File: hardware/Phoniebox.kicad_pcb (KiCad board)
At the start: 2 copper layers, 64.8 x 66 mm, 75 parts, among them J1 GPIO, J2 Screw_Terminal_01x08, J3 Screw_Terminal_01x08, J4 Screw_Terminal_01x08, J5 Conn_01x02, J6 Conn_02x06_Odd_Even, J8 Conn_01x08, Q1 2N7002, Q2 2N7002, Q3 2N7002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

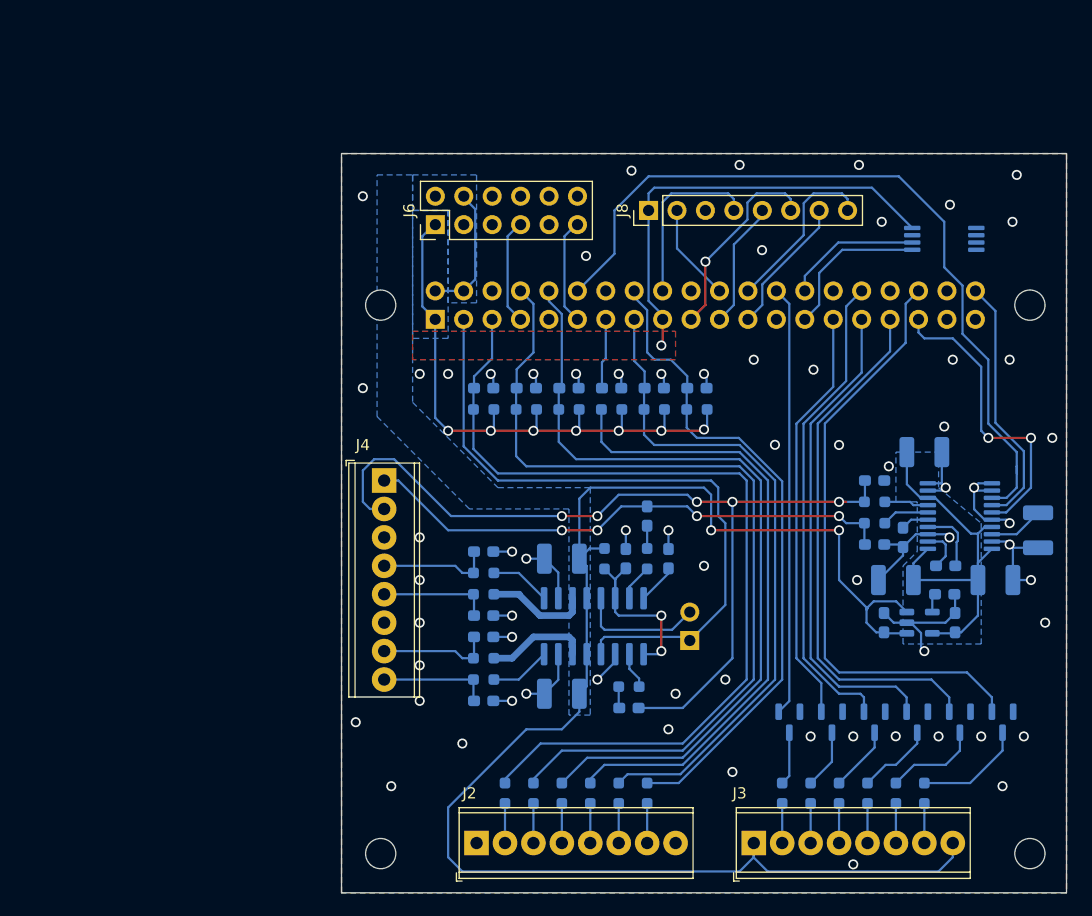
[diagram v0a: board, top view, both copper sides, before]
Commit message: Add OnOff-SHIM circuit to PCB
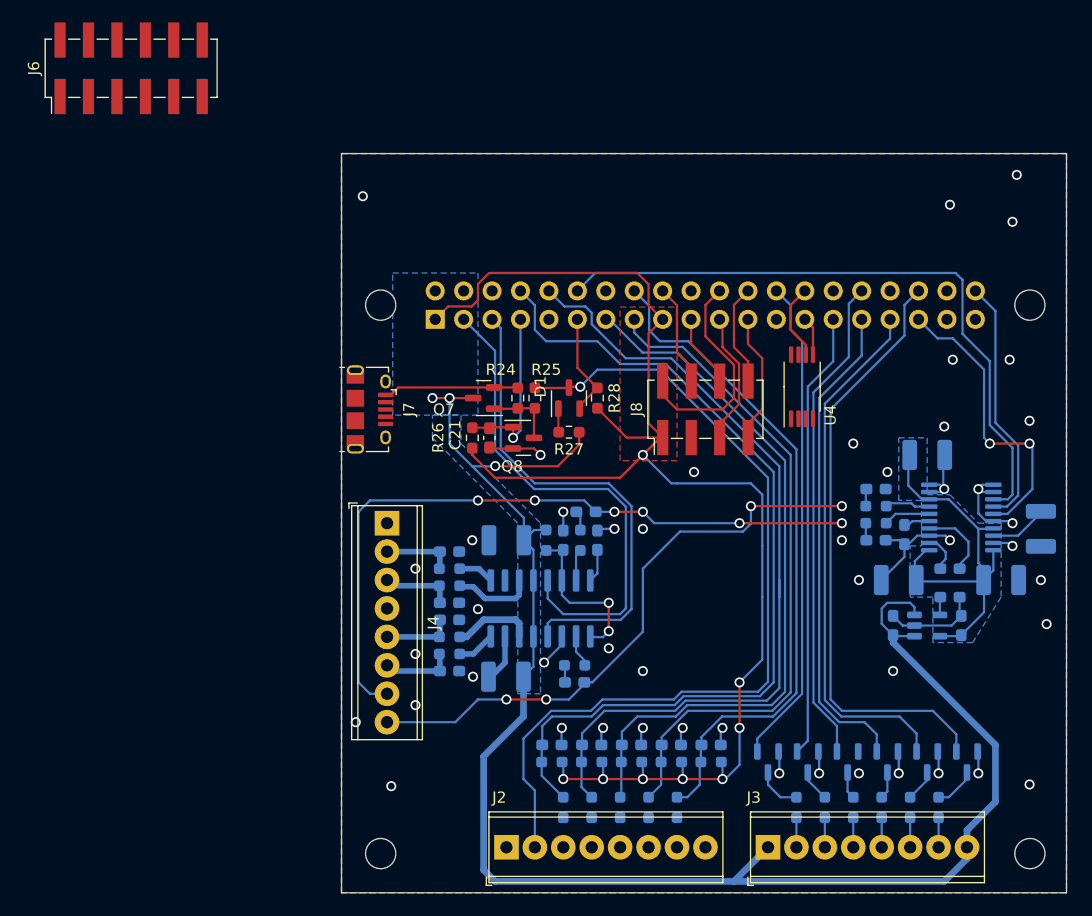
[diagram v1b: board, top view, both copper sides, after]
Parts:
- removed C1: 1n, Capacitor_SMD:C_0603_1608Metric_Pad1.08x0.95mm_HandSolder
- removed J5: Conn_01x02, Connector_PinHeader_2.54mm:PinHeader_1x02_P2.54mm_Vertical
- removed R1: 10k, Resistor_SMD:R_0603_1608Metric_Pad0.98x0.95mm_HandSolder
- removed R2: 100, Resistor_SMD:R_0603_1608Metric_Pad0.98x0.95mm_HandSolder
- added C21: 4u7, Capacitor_SMD:C_0603_1608Metric_Pad1.08x0.95mm_HandSolder, F.Cu at (113.2, 59.4)
- added D1: BAT54C, Package_TO_SOT_SMD:SOT-23, F.Cu at (120.3, 55.8)
- added J7: USB_B_Micro, Connector_USB:USB_Micro-B_Amphenol_10118194_Horizontal, F.Cu at (102.5, 56.8)
- added Q7: AO3401A, Package_TO_SOT_SMD:SOT-23, F.Cu at (112.7, 55.8)
- added Q8: 2N7002, Package_TO_SOT_SMD:SOT-23, F.Cu at (116.3, 59.4)
- added R24: 100k, Resistor_SMD:R_0603_1608Metric_Pad0.98x0.95mm_HandSolder, F.Cu at (115.7, 55.8)
- added R25: 10k, Resistor_SMD:R_0603_1608Metric_Pad0.98x0.95mm_HandSolder, F.Cu at (117.3, 55.8)
- added R26: 1k, Resistor_SMD:R_0603_1608Metric_Pad0.98x0.95mm_HandSolder, F.Cu at (111.7, 59.4)
- added R27: 1k, Resistor_SMD:R_0603_1608Metric_Pad0.98x0.95mm_HandSolder, F.Cu at (120.3, 58.9)
- added R28: 1k, Resistor_SMD:R_0603_1608Metric_Pad0.98x0.95mm_HandSolder, F.Cu at (122.9, 55.8)
- J6: footprint Connector_PinHeader_2.54mm:PinHeader_2x06_P2.54mm_Vertical -> Connector_PinHeader_2.54mm:PinHeader_2x06_P2.54mm_Vertical_SMD
- J8: value Conn_01x08 -> Conn_02x04_Odd_Even; footprint Connector_PinHeader_2.54mm:PinHeader_1x08_P2.54mm_Vertical -> Connector_PinHeader_2.54mm:PinHeader_2x04_P2.54mm_Vertical_SMD
- U4: moved to F.Cu
- moved C8 32.0 mm to (118.8, 86.8)
- moved C9 31.9 mm to (122.4, 86.8)
- moved C14 31.9 mm to (125.9, 86.8)
- moved C15 31.9 mm to (129.5, 86.8)
- moved C16 31.9 mm to (133.0, 86.8)
- moved R6 31.6 mm to (118.8, 88.3)
- moved R8 31.6 mm to (122.4, 88.3)
- moved R10 31.5 mm to (125.9, 88.3)
- moved R12 31.5 mm to (129.5, 88.3)
- moved R20 31.5 mm to (133.0, 88.3)
- moved J6 30.6 mm to (81.2, 26.3)
- moved J8 18.5 mm to (132.5, 56.8)
- moved U4 18.3 mm to (141.1, 54.8), turned to 90 degrees
- moved C6 6.56 mm to (122.9, 68.5)
- moved R3 6.19 mm to (121.3, 68.5)
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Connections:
- J1 pad 11: /Trigger -> /GPIO17_Trigger
- J1 pad 7: /Power_Cut -> /GPIO4_PowerOff
- J4 pad 1: /INL -> GND
- J4 pad 2: /INR -> /SPK_L+
- J4 pad 3: GND -> /SPK_L-
- J4 pad 4: /SPK_L+ -> GND
- J4 pad 5: /SPK_L- -> /SPK_R-
- J4 pad 6: GND -> /SPK_R+
- J4 pad 7: /SPK_R- -> /INL
- J4 pad 8: /SPK_R+ -> /INR
- U1 pad 12: /GPIO2 -> /GPIO3
- U1 pad 5: /~{MUTE} -> /GPIO2
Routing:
- net /Button_1: track 3.53 -> 77.8 mm, vias 0 -> 1
- net /GPIO3: track 81.3 -> 44.2 mm
- net +3V3: track 94.1 -> 125.5 mm
- net /INR: track 80.2 -> 54.5 mm, vias 5 -> 4
- net /INL: track 48.2 -> 64.9 mm, vias 4 -> 6
- net /GPIO4_PowerOff: track 0.00 -> 15.5 mm, vias 0 -> 1
- net /GPIO2: track 60.3 -> 45.0 mm
- net /GPIO18: track 70.6 -> 58.3 mm
- net /VBUS: track 0.00 -> 12.1 mm
- net /MOSI: track 18.0 -> 6.57 mm, vias 1 -> 0
- net /~{MUTE}: track 11.2 -> 0.00 mm
- net /RST: track 8.76 -> 19.7 mm
- net GND: track 79.8 -> 69.4 mm, vias 67 -> 47
- net /ID_SDA: track 13.8 -> 3.46 mm
- net /GPIO17_Trigger: track 0.00 -> 9.37 mm
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- removed copper zone on B.Cu, net +3V3

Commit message: Fix DRC errors/warnings, Add round edges for PCB.
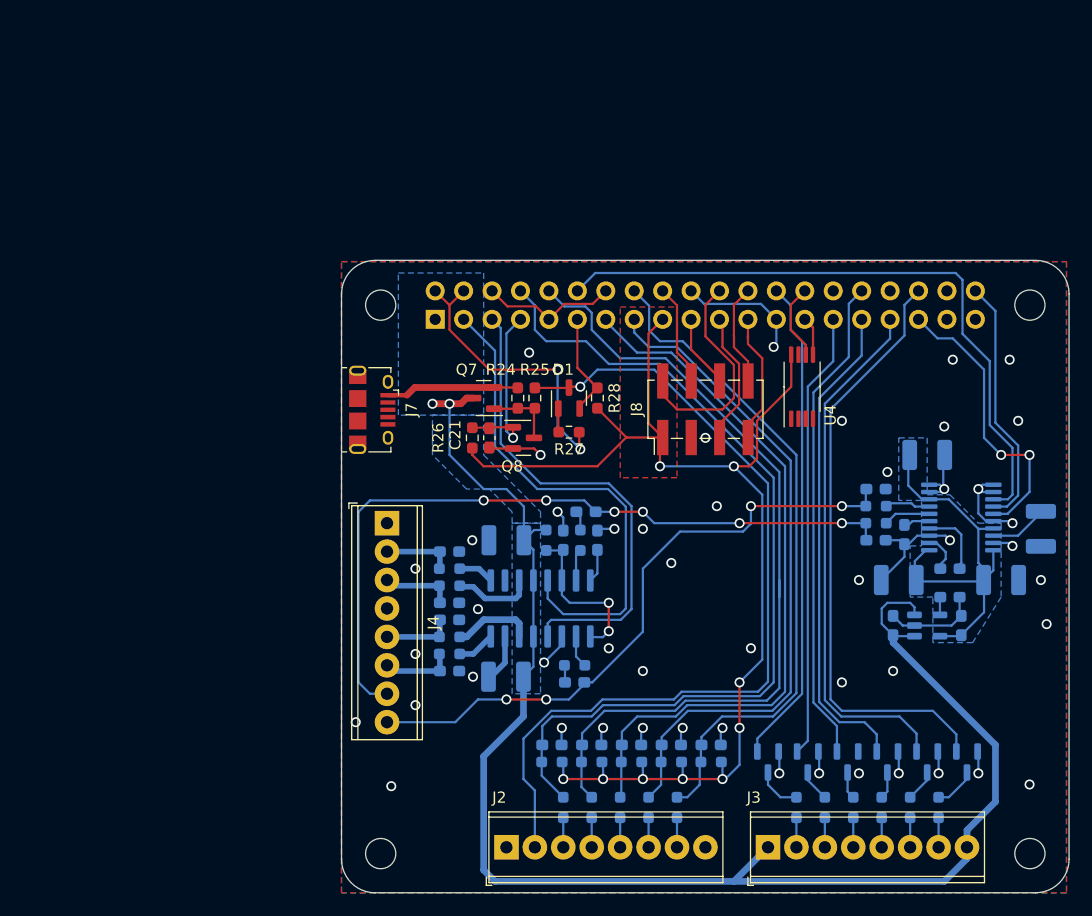
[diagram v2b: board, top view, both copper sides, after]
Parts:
- removed J6: Conn_02x06_Odd_Even, Connector_PinHeader_2.54mm:PinHeader_2x06_P2.54mm_Vertical_SMD
- moved J7 0.21 mm to (102.8, 56.8)
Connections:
- J1 pad 1: +3V3 -> unconnected-(J1-Pad1)
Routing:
- net GND: track 69.4 -> 92.3 mm, vias 47 -> 49
- net +3V3: track 125.5 -> 109.3 mm, vias 8 -> 9
- net +5V: track 146.9 -> 162.8 mm
- net /Button_6: track 0.00 -> 2.64 mm
- net /Button_5: track 0.00 -> 2.64 mm
- net /Button_4: track 0.00 -> 2.64 mm
- net /Button_3: track 0.00 -> 2.64 mm
- net /Button_2: track 0.00 -> 2.64 mm
- net /INR: track 54.5 -> 56.6 mm
- net /INL: track 64.9 -> 66.3 mm
- net /GPIO19: track 26.7 -> 25.9 mm
- net Net-(C24-Pad2): track 6.71 -> 6.18 mm
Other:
- board size 64.8 x 66 mm -> 65 x 56.5 mm

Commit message: Create hierachical schematic sheets for audio/LED/buttons.
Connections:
- net /AVDD renamed /Audio/AVDD
- net /INL1 renamed /Audio/INL1
- net /INL2 renamed /Audio/INL2
- net /INR1 renamed /Audio/INR1
- net /INR2 renamed /Audio/INR2
- net /LOUT+ renamed /Audio/LOUT+
- net /LOUT- renamed /Audio/LOUT-
- net /OUTL renamed /Audio/OUTL
- net /OUTR renamed /Audio/OUTR
- net /ROUT+ renamed /Audio/ROUT+
- net /ROUT- renamed /Audio/ROUT-
- net Net-(C25-Pad1) renamed /Audio/VNEG
- net Net-(C26-Pad1) renamed /Audio/LDOO

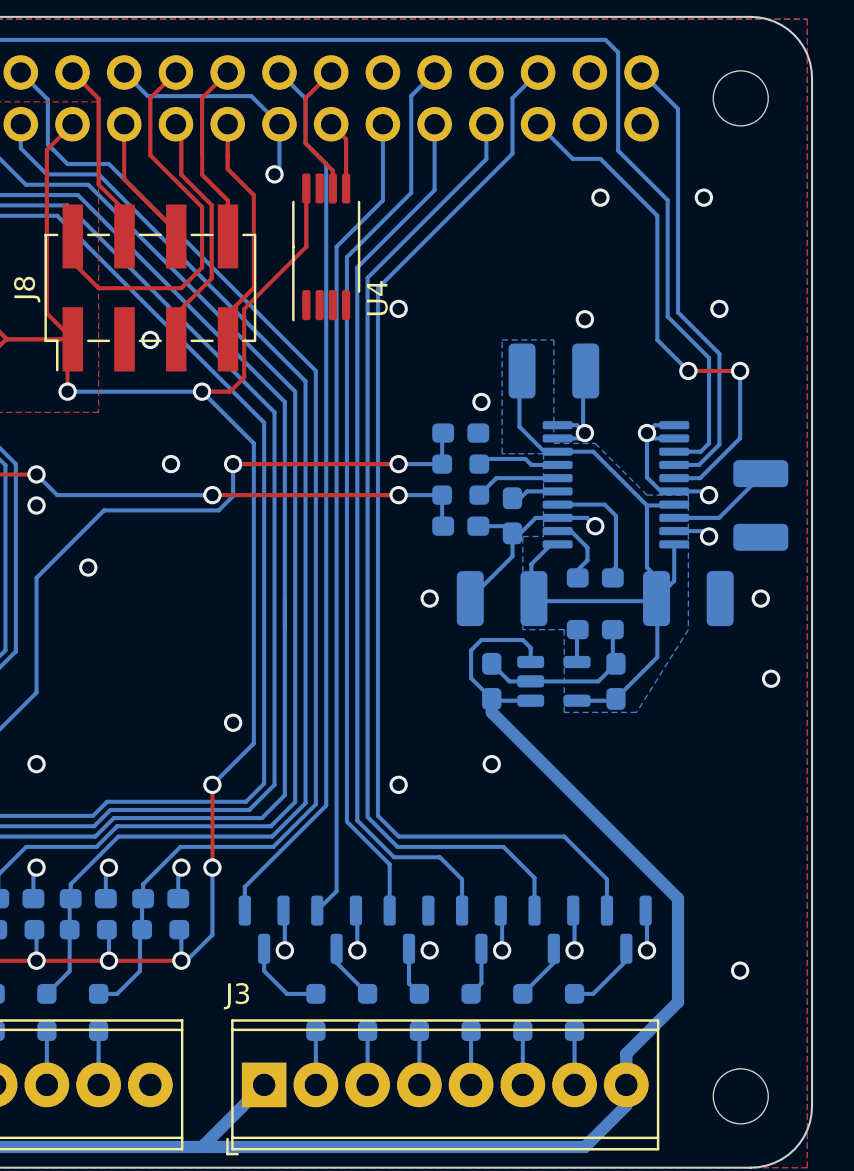
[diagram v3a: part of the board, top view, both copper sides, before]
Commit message: Place OnOffSHIM circuit on separate page.
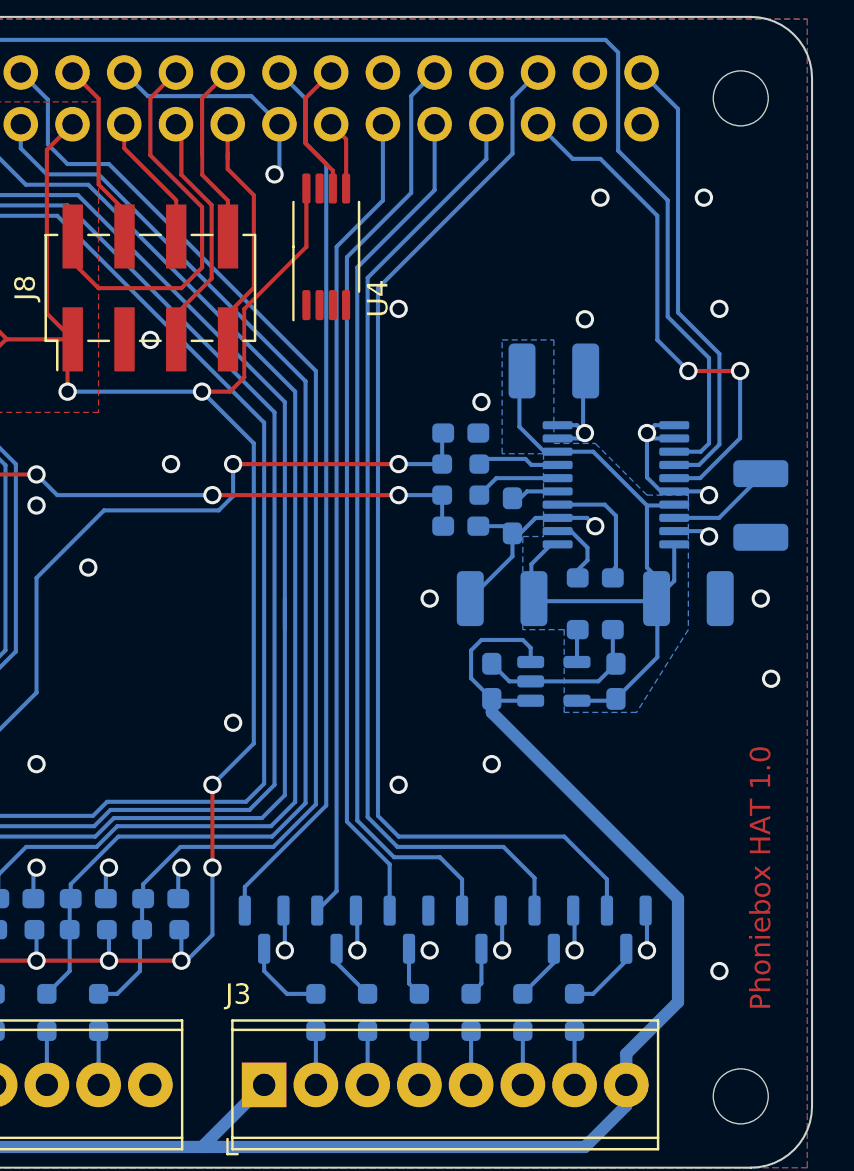
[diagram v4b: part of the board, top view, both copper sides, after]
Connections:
- net /Q7_G renamed /OnOffSHIM/Q7_G
- net /VBUS renamed /OnOffSHIM/VBUS
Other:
- board text added: "Phoniebox HAT 1.0"
